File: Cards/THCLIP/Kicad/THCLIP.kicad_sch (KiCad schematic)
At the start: 12 parts, among them J2 Conn_01x03_Pin, J3 Conn_01x05_Pin, K1 Relay_SPDT, U1 RS3K-2424S/H3

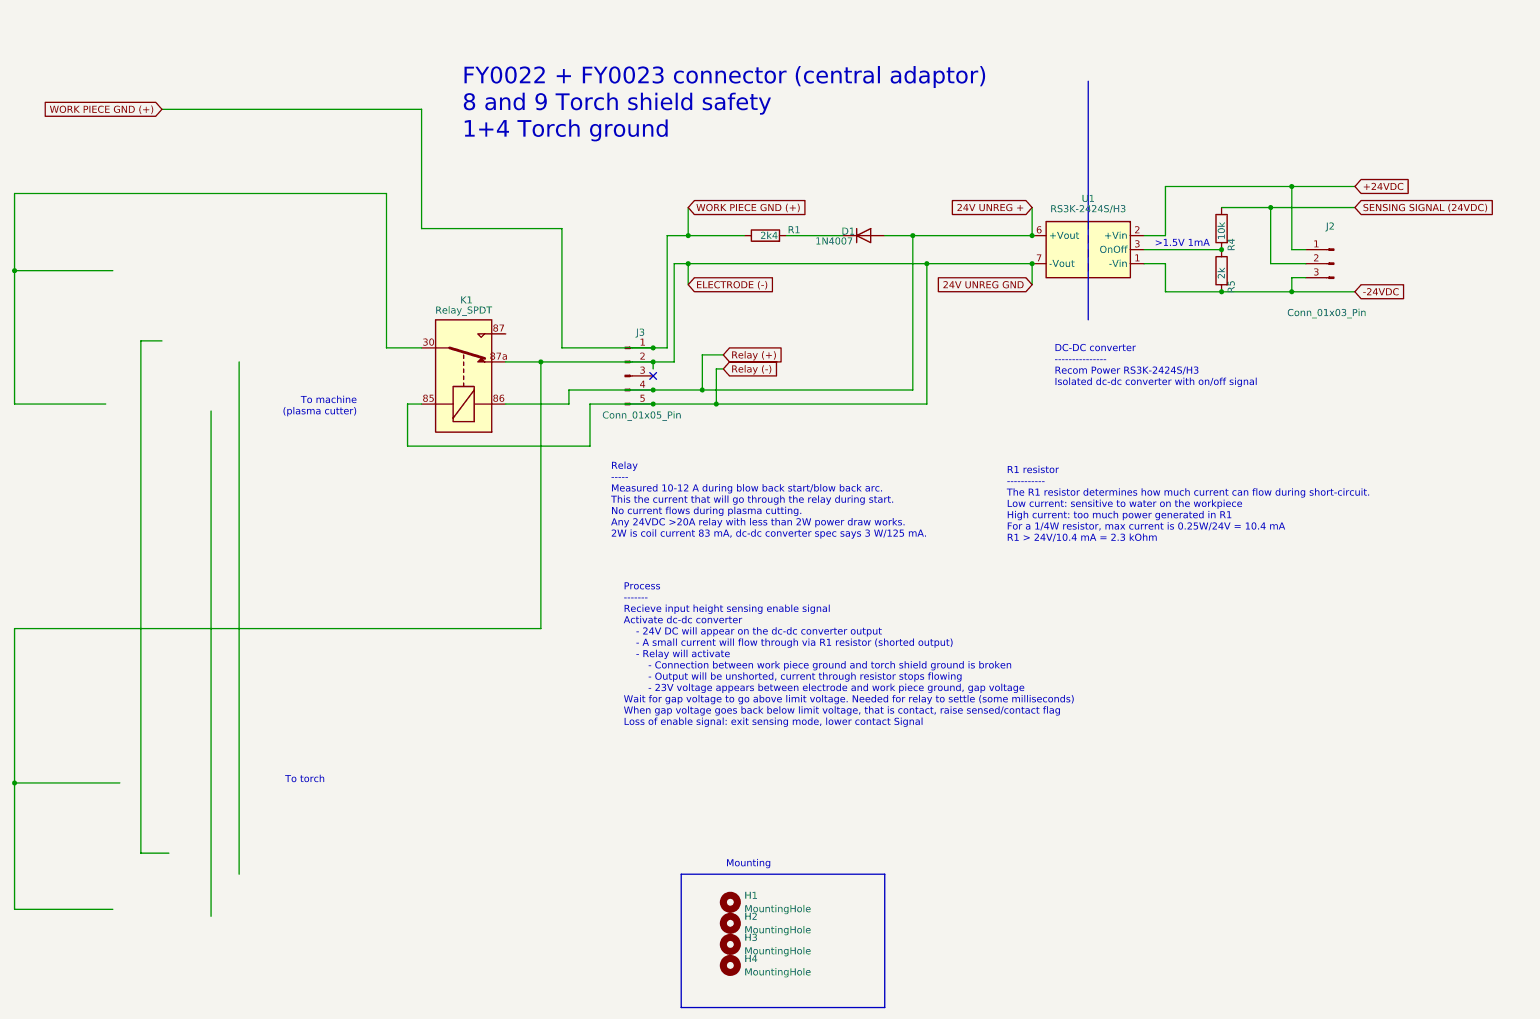
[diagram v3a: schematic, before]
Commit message: Updated to read voltage from ground clamp instead of ground in the plasma, which obviously isn't the´real thing.
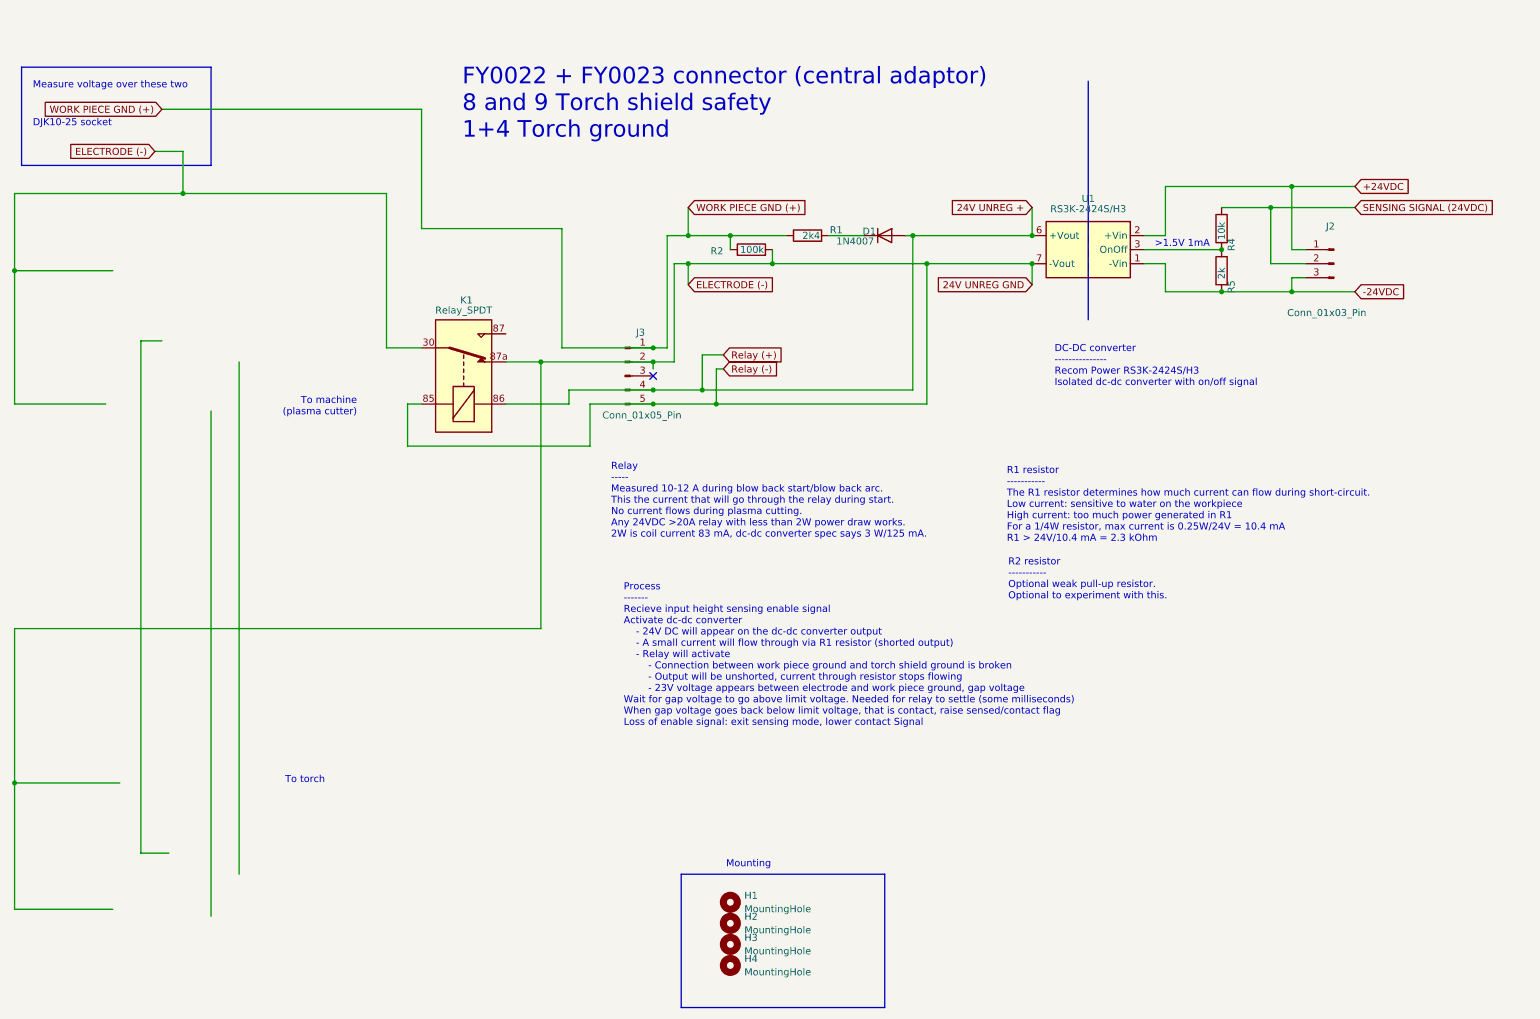
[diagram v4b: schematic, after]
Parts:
- added R2: 100k, Resistor_THT:R_Axial_DIN0207_L6.3mm_D2.5mm_P10.16mm_Horizontal, symbol Device:R
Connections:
- net 24V UNREG GND: now also K1.30, R2.2
- net WORK PIECE GND (+): now also R2.1
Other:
- note added: "DJK10-25 socket"
- note added: "Measure voltage over these two"
- note added: "R2 resistor ----------- Optional weak pull-up resistor. Optional to experiment with this."
- moved on the sheet: D1, R1
